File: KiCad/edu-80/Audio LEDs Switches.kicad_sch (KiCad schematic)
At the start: 29 parts, among them J1 Audio Out, J2 Audio In, Q3 ED1402, SW1 Clock Switch, SW1 Memory Protect, SW1 User Switch, U15 7400, U23 CA3130

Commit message: Working on removing edu-80-rescue symbol library
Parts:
- C100, C6, C7, C8, C9: symbol edu-80-rescue:CP1_Small-Device -> Edu-80_Symbols:CP1
- IND1, IND2, IND3: symbol edu-80-rescue:LED_ALT-Device -> Edu-80_Symbols:LED
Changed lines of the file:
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@@
     )
   )
-  (symbol (lib_id "edu-80-rescue:LED_ALT-Device") (at 214.63 100.33 180) (unit 1)
+  (symbol (lib_id "Edu-80_Symbols:LED") (at 214.63 100.33 180) (unit 1)
     (in_bom yes) (on_board yes) (dnp no)
     (property "Reference" "IND1" (at 214.8078 93.853 0)
@@
     )
   )
-  (symbol (lib_id "edu-80-rescue:LED_ALT-Device") (at 214.63 115.57 180) (unit 1)
+  (symbol (lib_id "Edu-80_Symbols:LED") (at 214.63 115.57 180) (unit 1)
     (in_bom yes) (on_board yes) (dnp no)
     (property "Reference" "IND2" (at 214.8078 109.093 0)
@@
     )
   )
-  (symbol (lib_id "edu-80-rescue:LED_ALT-Device") (at 214.63 130.81 180) (unit 1)
+  (symbol (lib_id "Edu-80_Symbols:LED") (at 214.63 130.81 180) (unit 1)
     (in_bom yes) (on_board yes) (dnp no)
     (property "Reference" "IND3" (at 214.8078 124.333 0)
@@
     )
   )
-  (symbol (lib_id "edu-80-rescue:CP1_Small-Device") (at 101.6 41.91 0) (unit 1)
+  (symbol (lib_id "Edu-80_Symbols:CP1") (at 101.6 41.91 0) (unit 1)
     (in_bom yes) (on_board yes) (dnp no)
     (property "Reference" "C7" (at 107.95 40.64 0)
@@
       (effects (font (size 1.27 1.27)) (justify right))
     )
-    (property "Footprint" "" (at 102.5652 45.72 0)
+    (property "Footprint" "" (at 101.6 41.91 0)
       (effects (font (size 1.27 1.27)) hide)
     )
@@
     )
   )
-  (symbol (lib_id "edu-80-rescue:CP1_Small-Device") (at 95.25 34.29 90) (unit 1)
+  (symbol (lib_id "Edu-80_Symbols:CP1") (at 95.25 34.29 90) (unit 1)
     (in_bom yes) (on_board yes) (dnp no)
     (property "Reference" "C6" (at 93.98 30.48 90)
@@
       (effects (font (size 1.27 1.27)) (justify right))
     )
-    (property "Footprint" "" (at 99.06 33.3248 0)
+    (property "Footprint" "" (at 95.25 34.29 0)
       (effects (font (size 1.27 1.27)) hide)
     )
@@
     )
   )
-  (symbol (lib_id "edu-80-rescue:CP1_Small-Device") (at 191.77 77.47 90) (unit 1)
+  (symbol (lib_id "Edu-80_Symbols:CP1") (at 191.77 77.47 90) (unit 1)
     (in_bom yes) (on_board yes) (dnp no)
     (property "Reference" "C8" (at 190.5 73.66 90)
@@
       (effects (font (size 1.27 1.27)) (justify right))
     )
-    (property "Footprint" "" (at 195.58 76.5048 0)
+    (property "Footprint" "" (at 191.77 77.47 0)
       (effects (font (size 1.27 1.27)) hide)
     )
@@
     )
   )
-  (symbol (lib_id "edu-80-rescue:CP1_Small-Device") (at 163.83 71.12 180) (unit 1)
+  (symbol (lib_id "Edu-80_Symbols:CP1") (at 163.83 71.12 180) (unit 1)
     (in_bom yes) (on_board yes) (dnp no)
     (property "Reference" "C9" (at 167.64 69.85 0)
@@
       (effects (font (size 1.27 1.27)) (justify right))
     )
-    (property "Footprint" "" (at 162.8648 67.31 0)
+    (property "Footprint" "" (at 163.83 71.12 0)
       (effects (font (size 1.27 1.27)) hide)
     )
@@
     )
   )
-  (symbol (lib_id "edu-80-rescue:CP1_Small-Device") (at 92.71 66.04 0) (unit 1)
+  (symbol (lib_id "Edu-80_Symbols:CP1") (at 92.71 66.04 0) (unit 1)
     (in_bom yes) (on_board yes) (dnp no)
     (property "Reference" "C100" (at 96.52 64.77 90)
@@
       (effects (font (size 1.27 1.27)) (justify right))
     )
-    (property "Footprint" "" (at 93.6752 69.85 0)
-      (effects (font (size 1.27 1.27)) hide)
-    )
+    (property "Footprint" "" (at 92.71 66.04 0)
+      (effects (font (size 1.27 1.27)) hide)
+    )

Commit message: Cleaning up the PAL-003 decoding, adding Modifications page.
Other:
- company: (none) -> Strangers
- title: (none) -> Edu-80 Z80 Trainer
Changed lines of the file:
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@@
 (kicad_sch (version 20230121) (generator eeschema)
   (paper "A")
+  (title_block
+    (title "Edu-80 Z80 Trainer")
+    (date "2023-06-03")
+    (rev "0.1")
+    (company "Strangers")
+    (comment 1 "Author: James D. Tucker")
+  )
   (junction (at 101.6 34.29) (diameter 0) (color 0 0 0 0)
   )

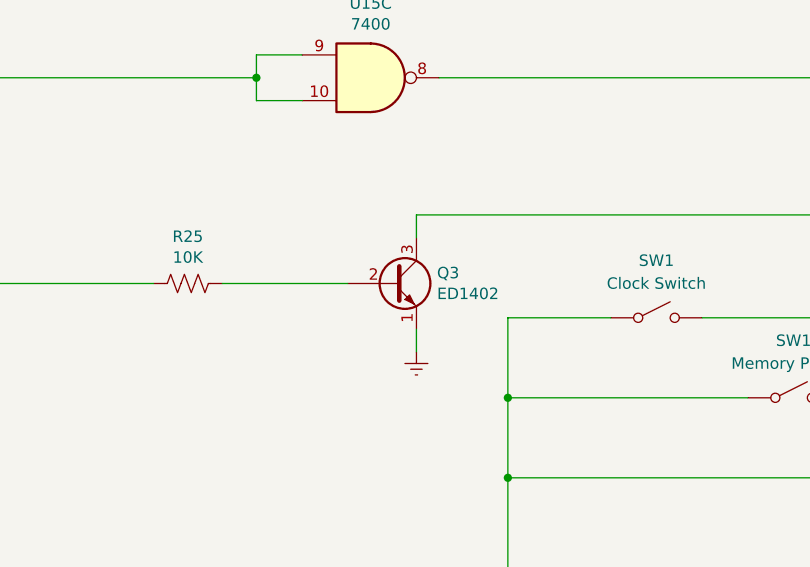
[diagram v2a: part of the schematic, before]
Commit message: Fixed ~IRQ vs. INT for PIO/CTC. Removed old (version 5) schematic files.
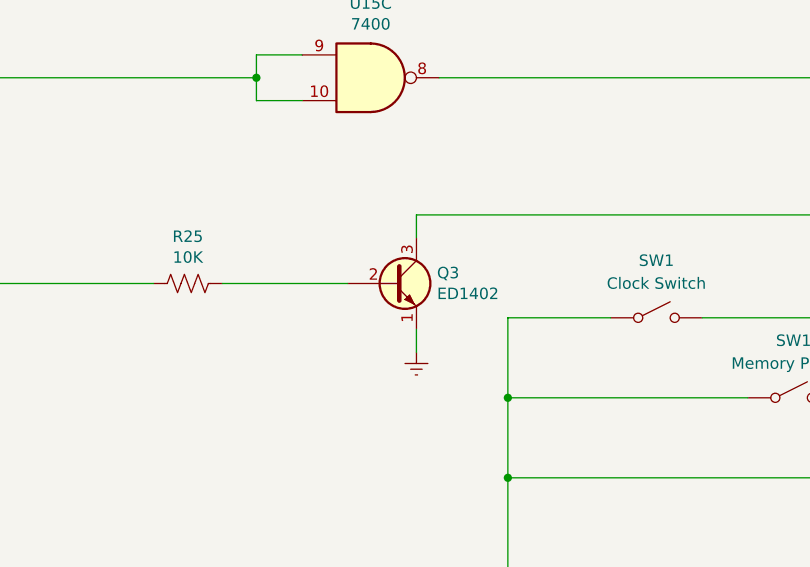
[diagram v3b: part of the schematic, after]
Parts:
- Q3: symbol Device:Q_NPN_EBC -> Edu-80_Symbols:Q_NPN_EBC
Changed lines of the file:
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@@
   (title_block
     (title "Edu-80 Z80 Trainer")
-    (date "2023-06-03")
+    (date "2023-06-05")
     (rev "0.1")
     (company "Strangers")
-    (comment 1 "Author: James D. Tucker")
+    (comment 4 "Author: James D. Tucker")
   )
   (junction (at 101.6 34.29) (diameter 0) (color 0 0 0 0)
@@
     )
   )
-  (symbol (lib_id "Device:Q_NPN_EBC") (at 101.6 138.43 0) (unit 1)
+  (symbol (lib_id "Edu-80_Symbols:Q_NPN_EBC") (at 101.6 138.43 0) (unit 1)
     (in_bom yes) (on_board yes) (dnp no)
     (property "Reference" "Q3" (at 106.426 137.2616 0)

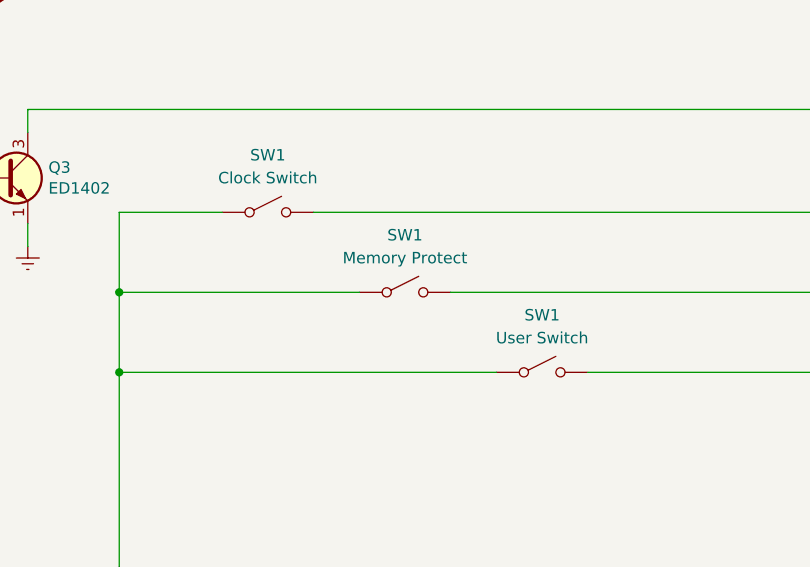
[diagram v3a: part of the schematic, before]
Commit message: Fixed the last of the EDR warnings/errors, adding footprints
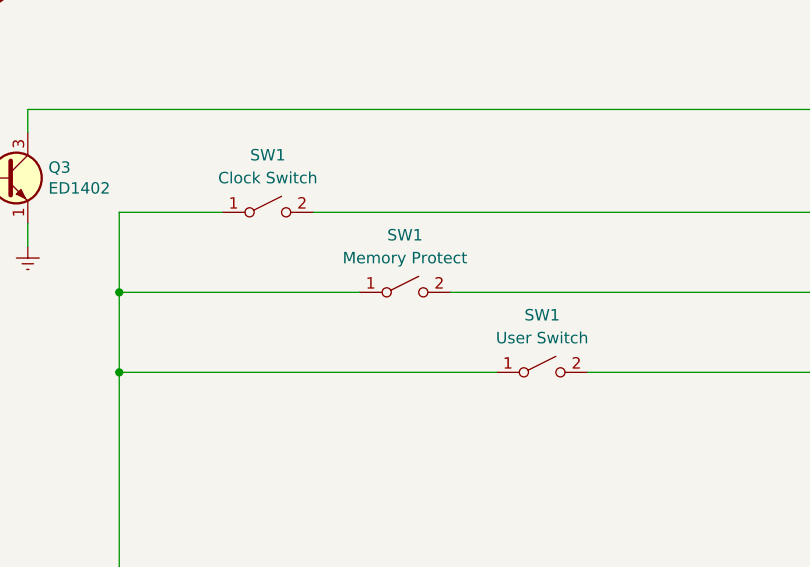
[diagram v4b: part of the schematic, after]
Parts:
- C100, C6, C7, C8, C9: footprint (none) -> Capacitor_THT:CP_Radial_D5.0mm_P2.50mm
- IND1, IND2, IND3: footprint (none) -> LED_THT:LED_D5.0mm
- Q3: footprint (none) -> Package_TO_SOT_THT:TO-92_Inline
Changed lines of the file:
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@@
       (effects (font (size 1.27 1.27)) (justify left))
     )
-    (property "Footprint" "" (at 106.68 135.89 0)
+    (property "Footprint" "Package_TO_SOT_THT:TO-92_Inline" (at 106.68 135.89 0)
       (effects (font (size 1.27 1.27)) hide)
     )
@@
       (effects (font (size 1.27 1.27)))
     )
-    (property "Footprint" "" (at 214.63 100.33 0)
+    (property "Footprint" "LED_THT:LED_D5.0mm" (at 214.63 100.33 0)
       (effects (font (size 1.27 1.27)) hide)
     )
@@
       (effects (font (size 1.27 1.27)))
     )
-    (property "Footprint" "" (at 214.63 115.57 0)
+    (property "Footprint" "LED_THT:LED_D5.0mm" (at 214.63 115.57 0)
       (effects (font (size 1.27 1.27)) hide)
     )
@@
       (effects (font (size 1.27 1.27)))
     )
-    (property "Footprint" "" (at 214.63 130.81 0)
+    (property "Footprint" "LED_THT:LED_D5.0mm" (at 214.63 130.81 0)
       (effects (font (size 1.27 1.27)) hide)
     )
@@
       (effects (font (size 1.27 1.27)) (justify right))
     )
-    (property "Footprint" "" (at 101.6 41.91 0)
+    (property "Footprint" "Capacitor_THT:CP_Radial_D5.0mm_P2.50mm" (at 101.6 41.91 0)
       (effects (font (size 1.27 1.27)) hide)
     )
@@
       (effects (font (size 1.27 1.27)) (justify right))
     )
-    (property "Footprint" "" (at 95.25 34.29 0)
+    (property "Footprint" "Capacitor_THT:CP_Radial_D5.0mm_P2.50mm" (at 95.25 34.29 0)
       (effects (font (size 1.27 1.27)) hide)
     )
@@
       (effects (font (size 1.27 1.27)) (justify right))
     )
-    (property "Footprint" "" (at 191.77 77.47 0)
+    (property "Footprint" "Capacitor_THT:CP_Radial_D5.0mm_P2.50mm" (at 191.77 77.47 0)
       (effects (font (size 1.27 1.27)) hide)
     )
@@
       (effects (font (size 1.27 1.27)) (justify right))
     )
-    (property "Footprint" "" (at 163.83 71.12 0)
+    (property "Footprint" "Capacitor_THT:CP_Radial_D5.0mm_P2.50mm" (at 163.83 71.12 0)
       (effects (font (size 1.27 1.27)) hide)
     )
@@
       (effects (font (size 1.27 1.27)) (justify right))
     )
-    (property "Footprint" "" (at 92.71 66.04 0)
-      (effects (font (size 1.27 1.27)) hide)
-    )
+    (property "Footprint" "Capacitor_THT:CP_Radial_D5.0mm_P2.50mm" (at 92.71 66.04 0)
+      (effects (font (size 1.27 1.27)) hide)
+    )

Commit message: Adding footprints.
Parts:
- C6, C7, C8, C9: footprint Capacitor_THT:CP_Radial_D5.0mm_P2.50mm -> Capacitor_THT:CP_Radial_D5.0mm_P2.00mm
- J1, J2: footprint (none) -> Connector_Audio:Jack_3.5mm_CUI_SJ-3523-SMT_Horizontal
- R113, R114, R19, R20, R21, R22, R23, R24, R25: footprint (none) -> Resistor_THT:R_Axial_DIN0204_L3.6mm_D1.6mm_P5.08mm_Horizontal
- R15, R16, R17, R18: footprint (none) -> Resistor_THT:R_Axial_DIN0309_L9.0mm_D3.2mm_P25.40mm_Horizontal
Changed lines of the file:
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@@
       (effects (font (size 1.27 1.27)) (justify right))
     )
-    (property "Footprint" "" (at 247.65 81.026 0)
+    (property "Footprint" "Connector_Audio:Jack_3.5mm_CUI_SJ-3523-SMT_Horizontal" (at 247.65 81.026 0)
       (effects (font (size 1.27 1.27)) hide)
     )
@@
       (effects (font (size 1.27 1.27)))
     )
-    (property "Footprint" "" (at 78.486 139.446 90)
+    (property "Footprint" "Resistor_THT:R_Axial_DIN0204_L3.6mm_D1.6mm_P5.08mm_Horizontal" (at 78.486 139.446 90)
       (effects (font (size 1.27 1.27)) hide)
     )
@@
       (effects (font (size 1.27 1.27)))
     )
-    (property "Footprint" "" (at 182.626 116.586 90)
+    (property "Footprint" "Resistor_THT:R_Axial_DIN0204_L3.6mm_D1.6mm_P5.08mm_Horizontal" (at 182.626 116.586 90)
       (effects (font (size 1.27 1.27)) hide)
     )
@@
       (effects (font (size 1.27 1.27)))
     )
-    (property "Footprint" "" (at 182.626 101.346 90)
+    (property "Footprint" "Resistor_THT:R_Axial_DIN0204_L3.6mm_D1.6mm_P5.08mm_Horizontal" (at 182.626 101.346 90)
       (effects (font (size 1.27 1.27)) hide)
     )
@@
       (effects (font (size 1.27 1.27)))
     )
-    (property "Footprint" "" (at 78.486 35.306 90)
+    (property "Footprint" "Resistor_THT:R_Axial_DIN0204_L3.6mm_D1.6mm_P5.08mm_Horizontal" (at 78.486 35.306 90)
       (effects (font (size 1.27 1.27)) hide)
     )
@@
       (effects (font (size 1.27 1.27)) (justify right))
     )
-    (property "Footprint" "Capacitor_THT:CP_Radial_D5.0mm_P2.50mm" (at 101.6 41.91 0)
+    (property "Footprint" "Capacitor_THT:CP_Radial_D5.0mm_P2.00mm" (at 101.6 41.91 0)
       (effects (font (size 1.27 1.27)) hide)
     )
@@
       (effects (font (size 1.27 1.27)))
     )
-    (property "Footprint" "" (at 111.506 35.306 90)
+    (property "Footprint" "Resistor_THT:R_Axial_DIN0204_L3.6mm_D1.6mm_P5.08mm_Horizontal" (at 111.506 35.306 90)
       (effects (font (size 1.27 1.27)) hide)
     )
@@
       (effects (font (size 1.27 1.27)))
     )
-    (property "Footprint" "" (at 124.206 42.164 90)
+    (property "Footprint" "Resistor_THT:R_Axial_DIN0309_L9.0mm_D3.2mm_P25.40mm_Horizontal" (at 124.206 42.164 90)
       (effects (font (size 1.27 1.27)) hide)
     )
@@
       (effects (font (size 1.27 1.27)) (justify right))
     )
-    (property "Footprint" "Capacitor_THT:CP_Radial_D5.0mm_P2.50mm" (at 95.25 34.29 0)
+    (property "Footprint" "Capacitor_THT:CP_Radial_D5.0mm_P2.00mm" (at 95.25 34.29 0)
       (effects (font (size 1.27 1.27)) hide)
     )
@@
       (effects (font (size 1.27 1.27)))
     )
-    (property "Footprint" "" (at 200.406 123.444 90)
+    (property "Footprint" "Resistor_THT:R_Axial_DIN0204_L3.6mm_D1.6mm_P5.08mm_Horizontal" (at 200.406 123.444 90)
       (effects (font (size 1.27 1.27)) hide)
     )
@@
       (effects (font (size 1.27 1.27)))
     )
-    (property "Footprint" "" (at 111.506 65.786 90)
+    (property "Footprint" "Resistor_THT:R_Axial_DIN0204_L3.6mm_D1.6mm_P5.08mm_Horizontal" (at 111.506 65.786 90)
       (effects (font (size 1.27 1.27)) hide)
     )
@@
       (effects (font (size 1.27 1.27)))
     )
-    (property "Footprint" "" (at 143.256 65.786 90)
+    (property "Footprint" "Resistor_THT:R_Axial_DIN0204_L3.6mm_D1.6mm_P5.08mm_Horizontal" (at 143.256 65.786 90)
       (effects (font (size 1.27 1.27)) hide)
     )
@@
       (effects (font (size 1.27 1.27)))
     )
-    (property "Footprint" "" (at 182.626 78.486 90)
+    (property "Footprint" "Resistor_THT:R_Axial_DIN0309_L9.0mm_D3.2mm_P25.40mm_Horizontal" (at 182.626 78.486 90)
       (effects (font (size 1.27 1.27)) hide)
     )
@@
       (effects (font (size 1.27 1.27)) (justify right))
     )
-    (property "Footprint" "Capacitor_THT:CP_Radial_D5.0mm_P2.50mm" (at 191.77 77.47 0)
+    (property "Footprint" "Capacitor_THT:CP_Radial_D5.0mm_P2.00mm" (at 191.77 77.47 0)
       (effects (font (size 1.27 1.27)) hide)
     )
@@
       (effects (font (size 1.27 1.27)))
     )
-    (property "Footprint" "" (at 143.764 59.944 90)
+    (property "Footprint" "Resistor_THT:R_Axial_DIN0309_L9.0mm_D3.2mm_P25.40mm_Horizontal" (at 143.764 59.944 90)
       (effects (font (size 1.27 1.27)) hide)
     )
@@
       (effects (font (size 1.27 1.27)) (justify right))
     )
-    (property "Footprint" "Capacitor_THT:CP_Radial_D5.0mm_P2.50mm" (at 163.83 71.12 0)
+    (property "Footprint" "Capacitor_THT:CP_Radial_D5.0mm_P2.00mm" (at 163.83 71.12 0)
       (effects (font (size 1.27 1.27)) hide)
     )
@@
       (effects (font (size 1.27 1.27)))
     )
-    (property "Footprint" "" (at 153.416 71.374 90)
+    (property "Footprint" "Resistor_THT:R_Axial_DIN0309_L9.0mm_D3.2mm_P25.40mm_Horizontal" (at 153.416 71.374 90)
       (effects (font (size 1.27 1.27)) hide)
     )
@@
       (effects (font (size 1.27 1.27)))
     )
-    (property "Footprint" "" (at 153.416 85.344 90)
+    (property "Footprint" "Resistor_THT:R_Axial_DIN0204_L3.6mm_D1.6mm_P5.08mm_Horizontal" (at 153.416 85.344 90)
       (effects (font (size 1.27 1.27)) hide)
     )
@@
       (effects (font (size 1.27 1.27)) (justify right))
     )
-    (property "Footprint" "" (at 247.65 37.846 0)
-      (effects (font (size 1.27 1.27)) hide)
-    )
+    (property "Footprint" "Connector_Audio:Jack_3.5mm_CUI_SJ-3523-SMT_Horizontal" (at 247.65 37.846 0)
+      (effects (font (size 1.27 1.27)) hide)
+    )
